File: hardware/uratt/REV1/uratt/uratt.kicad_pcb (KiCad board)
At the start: 4 copper layers, 62 x 97.4 mm, 161 parts, among them J1 USB_B_Micro, J2 Micro_SD_Card, J3 Conn_01x10, J4 Conn_01x04, J5 Conn_01x04, J6 Conn_01x02, J7 Conn_01x02, J8 Conn_01x02, J9 Conn_01x10, Q1 MMBT3904, Q2 MMBT3904, Q3 DMP31D0U, Q4 2N7002, SW1 SW_Push, SW2 SW_Push, SW3 SW_Push, SW4 SW_SPDT, U1 SN65220, U2 CP2102N-A01-GQFN24, U3 ESP32-WROOM-32, U4 MCP73832-2-OT, U5 TPS2115A, U6 TPS61032PWP, U7 AP2112K-3.3, U8 AP2112K-3.3, U9 MP6513

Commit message: work in progress on REV1 schematic/PCB
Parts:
- added C35: 100uF, Capacitor_SMD:CP_Elec_5x3, F.Cu at (0.25, 37.3)
- added Q5: 2N7002, Package_TO_SOT_SMD:SOT-23, F.Cu at (6.95, 36.2)
- added Q6: DMP31D0U, Package_TO_SOT_SMD:SOT-23, F.Cu at (6.95, 40.7)
- added R32: 1K, Resistor_SMD:R_0603_1608Metric, F.Cu at (-2.22, 42.0)
- added R33: 10K, Resistor_SMD:R_0603_1608Metric, F.Cu at (11.2, 35.2)
- added R56: 22.1K, Resistor_SMD:R_0603_1608Metric, F.Cu at (-1.52, 49.3)
- added R57: 47.5K, Resistor_SMD:R_0603_1608Metric, F.Cu at (-1.52, 51.8)
- added R58: 1K, Resistor_SMD:R_0603_1608Metric, F.Cu at (2.49, 49.3)
- added R59: 470, Resistor_SMD:R_0603_1608Metric, F.Cu at (11.2, 55.3)
- added R60: 1K, Resistor_SMD:R_0603_1608Metric, F.Cu at (1.79, 42.0)
- added R61: 10K, Resistor_SMD:R_0603_1608Metric, F.Cu at (19.3, 35.2)
- added TP8: TestPoint, TestPoint:TestPoint_Pad_D1.0mm, F.Cu at (10.8, 49.5)
- BZ2: value Buzzer (ALT OPT) -> Buzzer (ALT)
- C14, C16, C18, C19, C2, C32, C6, C7, C8, C9: value .1uF -> 0.1uF
- D1: value 1N5819 -> SD0805S020S1R0
- D2: value DT1240A-08LP3810 -> DT1240A-08LP3810-7
- FB4: value FB -> FB (OPTION)
- R51: value 220 -> 20
- R53: value 100 -> 10
- U1: value SN65220 -> SN65220DBVR
- U2: value CP2102N-A01-GQFN24 -> CP2102N-A02-GQFN24
- U3: value ESP32-WROOM-32 -> ESP32-WROOM-32E
- U4: value MCP73832-2-OT -> MCP73832T-2ACI/OT
- U5: value TPS2115A -> TPS2115APWR
- U7, U8: value AP2112K-3.3 -> AP2112K-3.3TRG1
- U9: value MP6513 -> MP6513GJ-Z
- moved TP2 54.2 mm to (18.8, 44.8)
- moved TP6 48.5 mm to (21.8, 54.6)
- moved TP1 43.4 mm to (15.7, 80.6)
- moved TP7 19.1 mm to (20.6, 67.3)
- moved TP4 11.8 mm to (20.1, 75.0)
- moved TP3 9.94 mm to (19.1, 89.2)
- renumbered R32 to 3M1, R33 to 510K1
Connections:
- D4 pad 3: Net-(D4-Pad3) -> EXP_SDA
- D5 pad 3: Net-(D5-Pad3) -> ALARM_SCL
- J5 pad 1: Net-(D5-Pad3) -> Net-(J5-Pad1)
- J5 pad 2: Net-(D4-Pad3) -> Net-(J5-Pad2)
- J7 pad 1: GND -> Net-(J7-Pad1)
- J7 pad 2: Net-(J7-Pad2) -> GND
- LCD1 pad 11: /Front Panel/R_LCD_3.3V -> GND1
- Q2 pad 2: /DTR -> DTR
- R12 pad 2: /DTR -> DTR
- R18 pad 1: GND -> SD_DAT0
- R18 pad 2: SD_DAT0 -> DTR
- R20 pad 1: Net-(D4-Pad3) -> Net-(J5-Pad2)
- R24 pad 1: Net-(D5-Pad3) -> Net-(J5-Pad1)
- R34 pad 2: PWR_ENABLE -> Net-(Q6-Pad3)
- SW4 pad 2: Net-(J7-Pad2) -> Net-(J7-Pad1)
- U2 pad 23: /DTR -> DTR
- U2 pad 8: +5VUSB -> Net-(R56-Pad1)
- U6 pad 8: GND -> +VSW
- U6 pad 9: PWR_ENABLE -> Net-(Q6-Pad3)
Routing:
- net DTR: track 0.00 -> 25.9 mm, vias 0 -> 2
- net /DTR: track 25.9 -> 0.00 mm, vias 2 -> 0
- net Net-(J7-Pad2): track 19.2 -> 0.00 mm
- net Net-(J7-Pad1): track 0.00 -> 18.3 mm
- net +10VSW: track 13.0 -> 0.00 mm, vias 2 -> 0
- net Net-(LCD1-Pad12): track 10.0 -> 0.00 mm, vias 2 -> 0
- net /Front Panel/R_LCD_3.3V: track 16.2 -> 11.6 mm, vias 7 -> 6
- net Net-(LCD1-Pad3): track 4.51 -> 0.00 mm
- net Net-(LCD1-Pad7): track 3.52 -> 0.00 mm
- net Net-(LCD1-Pad4): track 3.42 -> 0.00 mm
- net Net-(LCD1-Pad6): track 3.14 -> 0.00 mm
- net Net-(LCD1-Pad5): track 3.13 -> 0.00 mm
- net GND1: track 12.1 -> 8.94 mm, vias 9 -> 7
- net GND: track 92.9 -> 90.9 mm, vias 101 -> 99
- net +VBATT: track 32.9 -> 32.1 mm, vias 3 -> 2
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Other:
- board text added: "REV1 / 20201-XXX-XX"

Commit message: uratt REV1 work, remove front panel, place new parts, partial routing
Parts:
- removed BK1, BK2, BK3: BREAKAWAY, uratt:RATT_BITE
- removed BZ1: Buzzer, Buzzer_Beeper:Buzzer_CUI_CPT-9019S-SMT
- removed BZ2: Buzzer (ALT), Buzzer_Beeper:Buzzer_CUI_CPT-9019S-SMT
- removed the C32 at (74.4, 107.9)
- removed C33: 1uF, Capacitor_SMD:C_0603_1608Metric
- removed C34: 0.1uF, Capacitor_SMD:C_0603_1608Metric
- removed C35: 100uF, Capacitor_SMD:CP_Elec_5x3
- removed H5, H6, H7, H8: MountingHole, MountingHole:MountingHole_2.1mm
- removed J9: Conn_01x10, Connector_FFC-FPC:TE_1-1734839-0_1x10-1MP_P0.5mm_Horizontal
- removed LCD1: ER-TFT0.96-1, uratt:ER-TFT0.96-1
- removed the Q4 at (71.1, 115.1)
- removed Q5: 2N7002, Package_TO_SOT_SMD:SOT-23
- removed the R11 at (51.1, 57.7)
- removed the R43 at (74.4, 111.0)
- removed the R44 at (65.1, 115.9)
- removed the R45 at (58.5, 115.9)
- removed the R46 at (58.5, 107.7)
- removed the R47 at (58.5, 104.6)
- removed the R48 at (58.5, 109.2)
- removed the R49 at (58.5, 106.2)
- removed the R50 at (58.5, 103.1)
- removed R51: 20, Resistor_SMD:R_0603_1608Metric
- removed R52, R58: 1K, Resistor_SMD:R_0603_1608Metric
- removed R53: 10, Resistor_SMD:R_0603_1608Metric
- removed R59: 470, Resistor_SMD:R_0603_1608Metric
- removed R61: 10K, Resistor_SMD:R_0603_1608Metric
- removed the SW3 at (77.5, 112.3)
- added C21: 100uF, Capacitor_SMD:CP_Elec_5x3, F.Cu at (65.5, 78.0)
- added R12: 1K, Resistor_SMD:R_0603_1608Metric, F.Cu at (62.8, 55.8)
- added R14: 0, Resistor_SMD:R_0603_1608Metric, F.Cu at (51.1, 57.7)
- J3: footprint Connector_FFC-FPC:TE_1-1734839-0_1x10-1MP_P0.5mm_Horizontal -> uratt:TE_1-1734742-0
- L1: footprint Inductor_SMD:L_12x12mm_H4.5mm -> Inductor_SMD:L_6.3x6.3_H3
- Q3: value DMP31D0U -> 2N7002; moved to F.Cu
- TP1, TP2, TP3, TP4, TP5: moved to F.Cu
- TP6: renamed from TP7; moved to F.Cu
- TP8: renamed from TP6; moved to F.Cu
- moved R37 63.4 mm to (52.2, 74.5), turned to 90 degrees
- moved R41 57.5 mm to (47.0, 77.5)
- moved R39 56.8 mm to (47.0, 79.2), turned to 180 degrees
- moved R10 54.0 mm to (52.2, 54.5)
- moved R11 53.8 mm to (52.2, 53.0)
- moved Q4 52.4 mm to (46.8, 74.8), turned to 180 degrees
- moved TP5 49.4 mm to (5.75, 32.2)
- moved Q3 36.6 mm to (46.8, 81.8), turned to 180 degrees
- moved R42 16.4 mm to (50.5, 74.5)
- moved R31 13.0 mm to (68.3, 89.0), turned to 90 degrees
- moved C19 11.3 mm to (66.8, 89.0)
- moved C31 7.30 mm to (41.7, 71.9)
- moved C32 7.30 mm to (42.0, 69.8)
- moved L1 5.59 mm to (41.2, 79.0)
- moved C25 5.01 mm to (62.0, 82.5), turned to 270 degrees
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- renumbered C21 to C22, C22 to C23, C25 to C24, C26 to C25, C23 to C26, C24 to C27, C27 to C28, C28 to C29, C29 to C30, C30 to C31, C31 to C32, D9 to D10, D10 to D11, D11 to D12, D4 to D2, D2 to D3, D3 to D4, D12 to D7, D7 to D8, D8 to D9, FB3 to FB2, FB2 to FB3, Q6 to Q4, R56 to R10, R57 to R11, R10 to R13, R12 to R15, R13 to R16, R14 to R17, R15 to R18, R16 to R19, R17 to R20, R18 to R21, R54 to R22, R55 to R23, R20 to R24, R19 to R25, R24 to R26, R21 to R27, R22 to R28, R23 to R29, R25 to R30, R26 to R31, R27 to R32, R28 to R33, R29 to R34, R30 to R35, R31 to R36, R32 to R37, R35 to R38, R33 to R39, R36 to R40, R60 to R41, R34 to R42, R37 to R43, R38 to R44, 3M1 to R45, 510K1 to R46, R39 to R47, R40 to R48, R41 to R49, R42 to R50, SW4 to SW3, TP8 to TP7, U7 to U6, U8 to U7, U6 to U8
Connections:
- Q3 pad 2: Net-(Q3-Pad2) -> GND
- Q3 pad 3: /Front Panel/R_LCD_3.3V -> Net-(Q3-Pad3)
- R37 pad 1: Net-(Q5-Pad1) -> Net-(Q3-Pad1)
- R39 pad 1: Net-(Q5-Pad3) -> Net-(Q3-Pad3)
- R41 pad 2: Net-(Q5-Pad3) -> Net-(Q3-Pad3)
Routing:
- net +5VSW: track 112.5 -> 61.0 mm, vias 11 -> 9
- net PWR_ENABLE: track 120.8 -> 74.9 mm, vias 6 -> 4
- net +3.3VSW: track 129.0 -> 104.1 mm, vias 19 -> 16
- net +VSW: track 54.8 -> 30.6 mm, vias 13 -> 8
- net Net-(BZ1-Pad1): track 21.2 -> 0.00 mm, vias 2 -> 0
- net Net-(BZ1-Pad2): track 20.5 -> 0.00 mm, vias 2 -> 0
- net Net-(D4-Pad3) (its old number): track 18.0 -> 0.00 mm, vias 1 -> 0
- net Net-(D4-Pad3): track 17.9 -> 35.9 mm, vias 2 -> 3
- net /Front Panel/R_LCD_BL: track 17.8 -> 0.00 mm, vias 2 -> 0
- net /Front Panel/R_BEEPER: track 17.1 -> 0.00 mm
- net /Front Panel/R_BTN: track 15.9 -> 0.00 mm
- net Net-(R10-Pad1): track 0.00 -> 15.6 mm, vias 0 -> 2
- net /Front Panel/R_LCD_CS: track 13.8 -> 0.00 mm, vias 2 -> 0
- net Net-(C32-Pad1): track 12.6 -> 0.00 mm, vias 1 -> 0
- net /Front Panel/R_LCD_3.3V: track 11.6 -> 0.00 mm, vias 6 -> 0
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- removed copper zone on B.Cu, net GND1
- removed copper zone on F.Cu, net GND1
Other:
- board size 62 x 97.4 mm -> 62 x 71.4 mm
- board text removed: "REV 0 / 2020-DEC-22"
- board text removed: "µRATT DOOR LOCK CONTROLLER - FRONT PANEL"

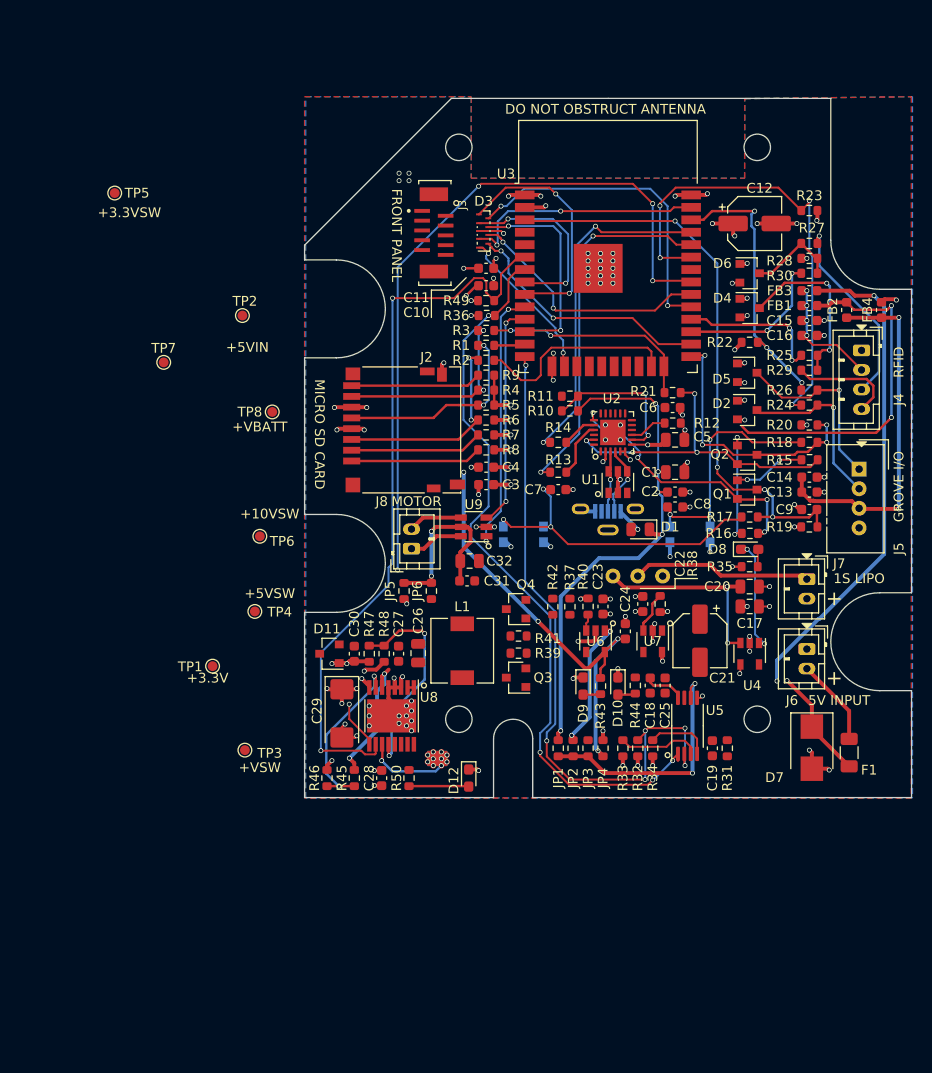
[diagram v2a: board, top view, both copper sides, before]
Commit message: uRATT REV1 progress.  placed and mostly routed.
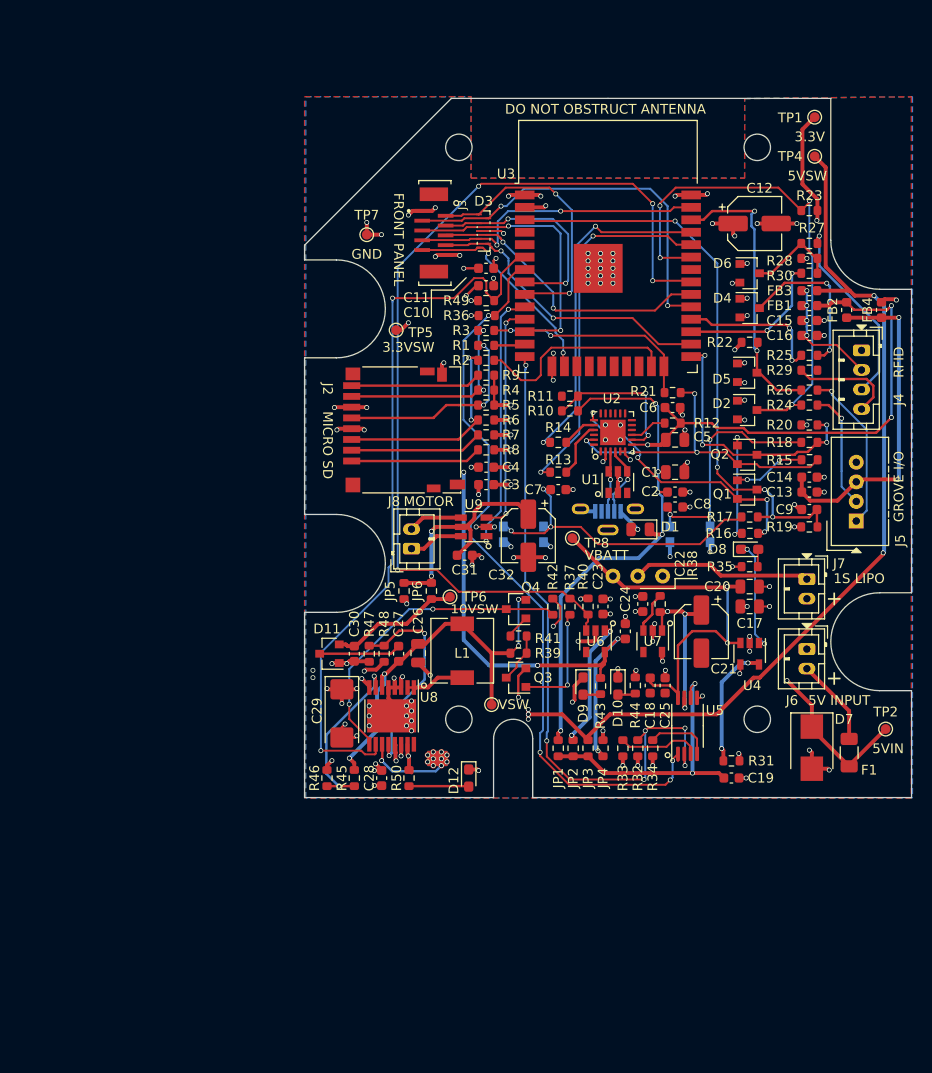
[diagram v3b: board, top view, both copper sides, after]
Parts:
- C32: value 10uF -> 100uF; footprint Capacitor_SMD:C_0805_2012Metric -> Capacitor_SMD:CP_Elec_5x3
- moved TP1 83.2 mm to (77.2, 24.5)
- moved TP2 78.1 mm to (84.5, 87.0)
- moved TP4 73.7 mm to (77.2, 28.5)
- moved TP8 33.3 mm to (52.5, 67.5)
- moved TP5 32.0 mm to (34.5, 46.2)
- moved TP3 25.6 mm to (44.2, 84.5)
- moved TP7 24.5 mm to (31.5, 36.5)
- moved TP6 20.4 mm to (40.0, 73.5)
- moved C32 6.53 mm to (48.0, 67.2), turned to 270 degrees
- moved J5 5.31 mm to (81.5, 65.8), turned to 180 degrees
- moved C19 3.61 mm to (68.8, 92.0), turned to 0 degrees
- moved C31 2.63 mm to (41.5, 69.2)
- moved R31 1.36 mm to (68.8, 90.2), turned to 180 degrees
- moved C21 0.94 mm to (65.7, 77.0)
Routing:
- net +5VSW: track 61.0 -> 112.1 mm, vias 9 -> 16
- net +VSW: track 30.6 -> 74.5 mm, vias 8 -> 12
- net Net-(Q4-Pad3): track 4.95 -> 32.1 mm, vias 1 -> 2
- net +3.3VSW: track 104.1 -> 125.6 mm, vias 16 -> 19
- net PWR_ENABLE: track 74.9 -> 96.2 mm
- net GND: track 81.8 -> 102.7 mm, vias 90 -> 100
- net Net-(D4-Pad3): track 35.9 -> 16.4 mm, vias 3 -> 2
- net Net-(D5-Pad3): track 18.7 -> 0.00 mm, vias 1 -> 0
- net +VBATT: track 24.8 -> 42.1 mm
- net Net-(J5-Pad1): track 0.00 -> 16.7 mm, vias 0 -> 1
- net +10VSW: track 0.00 -> 13.5 mm
- net Net-(R31-Pad2): track 0.00 -> 12.8 mm, vias 0 -> 2
- net +3V3: track 20.5 -> 32.7 mm, vias 18 -> 20
- net Net-(J5-Pad2): track 0.00 -> 12.1 mm, vias 0 -> 1
- net Net-(Q3-Pad1): track 0.00 -> 11.6 mm, vias 0 -> 2
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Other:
- board text added: "10VSW"
- board text added: "3.3V"
- board text added: "3.3VSW"
- board text added: "5VIN"
- board text added: "5VSW"
- board text added: "GND"
- board text added: "MICRO SD"
- board text added: "VBATT"
- board text added: "VSW"
- board text removed: "+10VSW"
- board text removed: "+3.3V"
- board text removed: "+3.3VSW"
- board text removed: "+5VIN"
- board text removed: "+5VSW"
- board text removed: "+VBATT"
- board text removed: "+VSW"
- board text removed: "MICRO SD CARD"

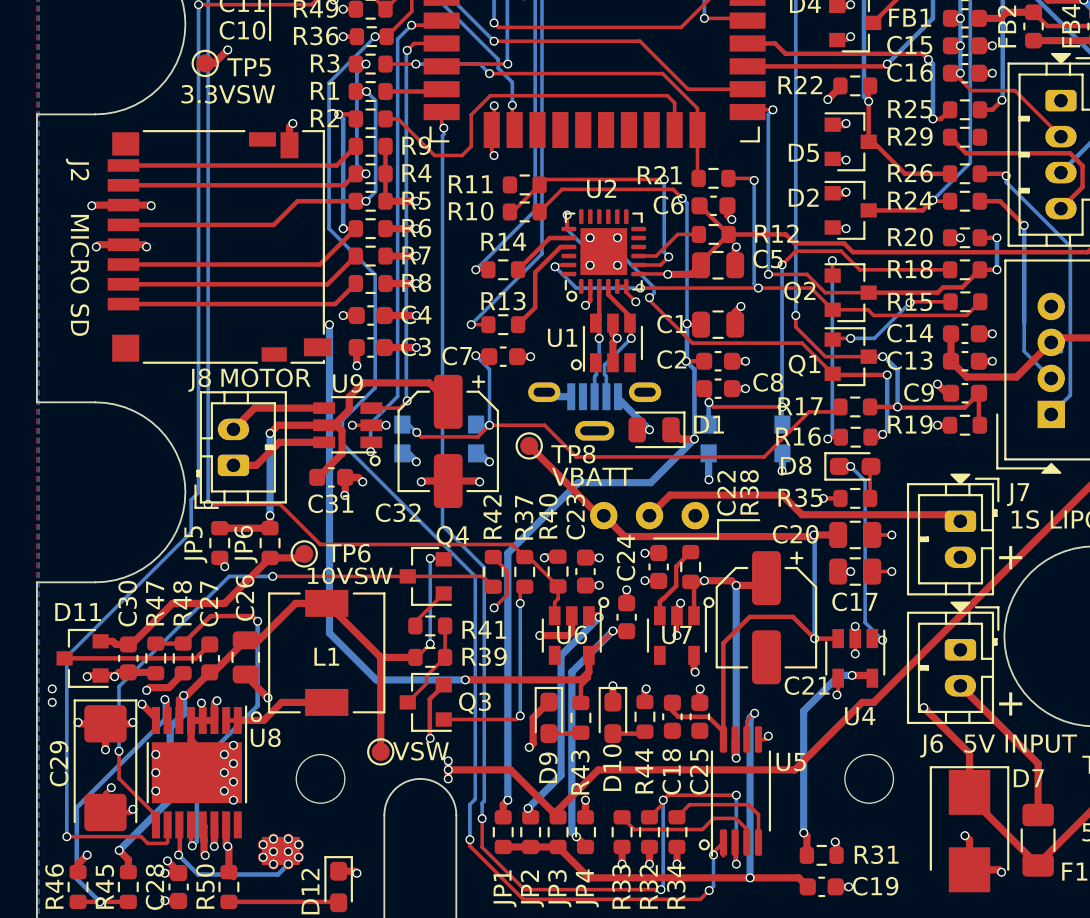
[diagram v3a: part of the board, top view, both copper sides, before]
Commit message: passes drc
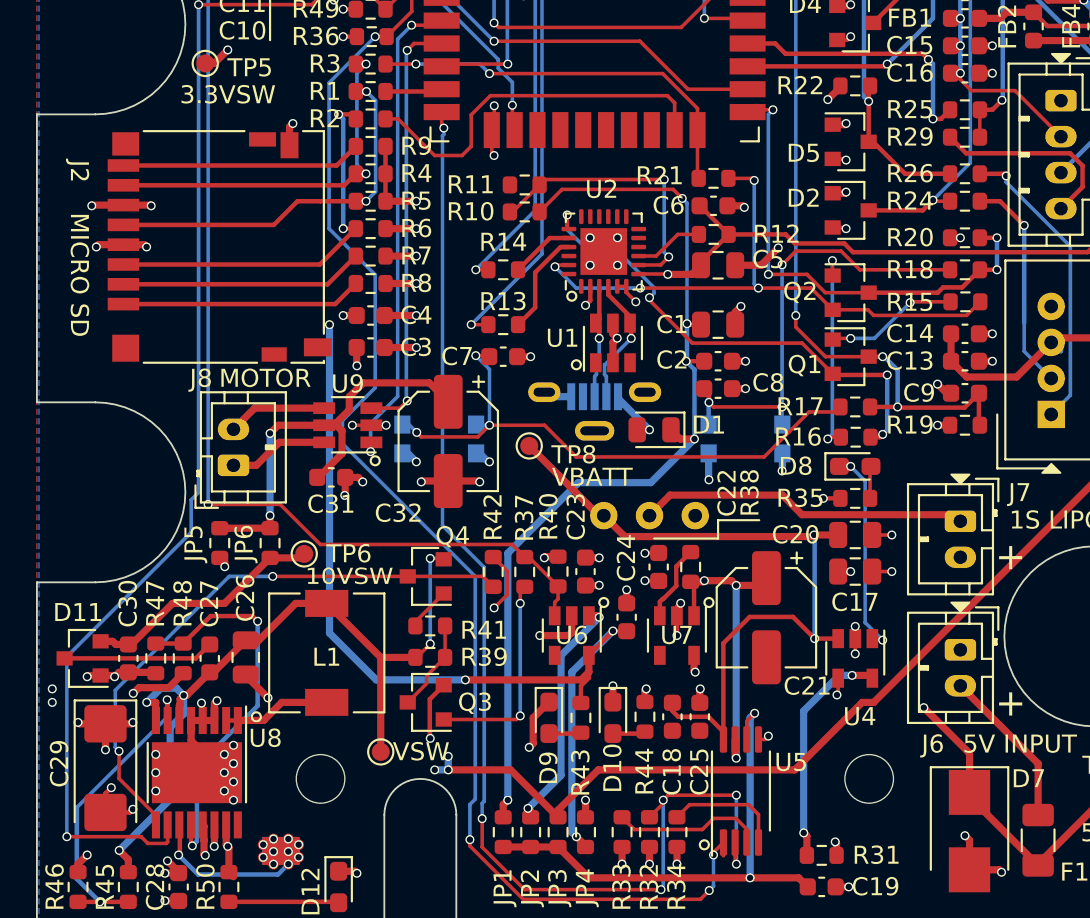
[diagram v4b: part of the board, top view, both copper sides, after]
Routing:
- net +VSW: track 74.5 -> 77.3 mm
- net GND: track 102.7 -> 105.4 mm
- net Net-(D4-Pad3): track 16.4 -> 17.9 mm
- net +5VSW: track 112.1 -> 112.6 mm
- removed copper zone on In1.Cu, net /Front Panel/R_LCD_3.3V
- removed copper zone on In2.Cu, net GND1
